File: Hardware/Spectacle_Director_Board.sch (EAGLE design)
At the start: 56 parts, among them J1 AUDIO-JACK3, J2 CORTEX_DEBUGPTH, Q1 2N7002PW, Q2 2N7002PW, U3 AP2112K-3.3V, U4 ATSAMD21G-A, U5 W25Q32FVSS

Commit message: Optimizing routing
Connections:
- new net USB_ID: JP15.ID
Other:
- moved on the sheet: JP15
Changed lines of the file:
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@@
 <instance part="GND26" gate="1" x="30.48" y="149.86"/>
 <instance part="F1" gate="G$1" x="38.1" y="175.26"/>
-<instance part="JP15" gate="G$1" x="20.32" y="167.64" rot="MR0"/>
+<instance part="JP15" gate="G$1" x="20.32" y="162.56" rot="MR0"/>
 <instance part="GND15" gate="1" x="73.66" y="160.02"/>
 <instance part="C7" gate="G$1" x="68.58" y="167.64" rot="MR0"/>
@@
 <segment>
 <pinref part="GND26" gate="1" pin="GND"/>
-<wire x1="30.48" y1="162.56" x2="30.48" y2="152.4" width="0.1524" layer="91"/>
-<wire x1="30.48" y1="162.56" x2="27.94" y2="162.56" width="0.1524" layer="91"/>
+<wire x1="30.48" y1="157.48" x2="30.48" y2="152.4" width="0.1524" layer="91"/>
+<wire x1="30.48" y1="157.48" x2="27.94" y2="157.48" width="0.1524" layer="91"/>
 <pinref part="JP15" gate="G$1" pin="GND"/>
 </segment>
@@
 <net name="VUSB" class="0">
 <segment>
-<wire x1="27.94" y1="172.72" x2="30.48" y2="172.72" width="0.1524" layer="91"/>
-<wire x1="30.48" y1="172.72" x2="30.48" y2="175.26" width="0.1524" layer="91"/>
+<wire x1="27.94" y1="167.64" x2="30.48" y2="167.64" width="0.1524" layer="91"/>
+<wire x1="30.48" y1="167.64" x2="30.48" y2="175.26" width="0.1524" layer="91"/>
 <wire x1="30.48" y1="175.26" x2="33.02" y2="175.26" width="0.1524" layer="91"/>
 <pinref part="F1" gate="G$1" pin="1"/>
@@
 <segment>
 <pinref part="JP15" gate="G$1" pin="SHIELD"/>
-<wire x1="12.7" y1="167.64" x2="10.16" y2="167.64" width="0.1524" layer="91"/>
-<label x="10.16" y="167.64" size="1.27" layer="95" rot="R180" xref="yes"/>
+<wire x1="12.7" y1="162.56" x2="10.16" y2="162.56" width="0.1524" layer="91"/>
+<label x="10.16" y="162.56" size="1.27" layer="95" rot="R180" xref="yes"/>
 </segment>
 </net>
@@
 <segment>
 <pinref part="JP15" gate="G$1" pin="D+"/>
-<wire x1="27.94" y1="167.64" x2="30.48" y2="167.64" width="0.1524" layer="91"/>
-<label x="30.48" y="167.64" size="1.27" layer="95" xref="yes"/>
+<wire x1="27.94" y1="162.56" x2="30.48" y2="162.56" width="0.1524" layer="91"/>
+<label x="30.48" y="162.56" size="1.27" layer="95" xref="yes"/>
 </segment>
 </net>
@@
 <segment>
 <pinref part="JP15" gate="G$1" pin="D-"/>
-<wire x1="27.94" y1="170.18" x2="30.48" y2="170.18" width="0.1524" layer="91"/>
-<label x="30.48" y="170.18" size="1.27" layer="95" xref="yes"/>
+<wire x1="27.94" y1="165.1" x2="30.48" y2="165.1" width="0.1524" layer="91"/>
+<label x="30.48" y="165.1" size="1.27" layer="95" xref="yes"/>
 </segment>
 </net>
@@
 </segment>
 </net>
+<net name="USB_ID" class="0">
+<segment>
+<pinref part="JP15" gate="G$1" pin="ID"/>
+<wire x1="27.94" y1="160.02" x2="30.48" y2="160.02" width="0.1524" layer="91"/>
+</segment>
+</net>

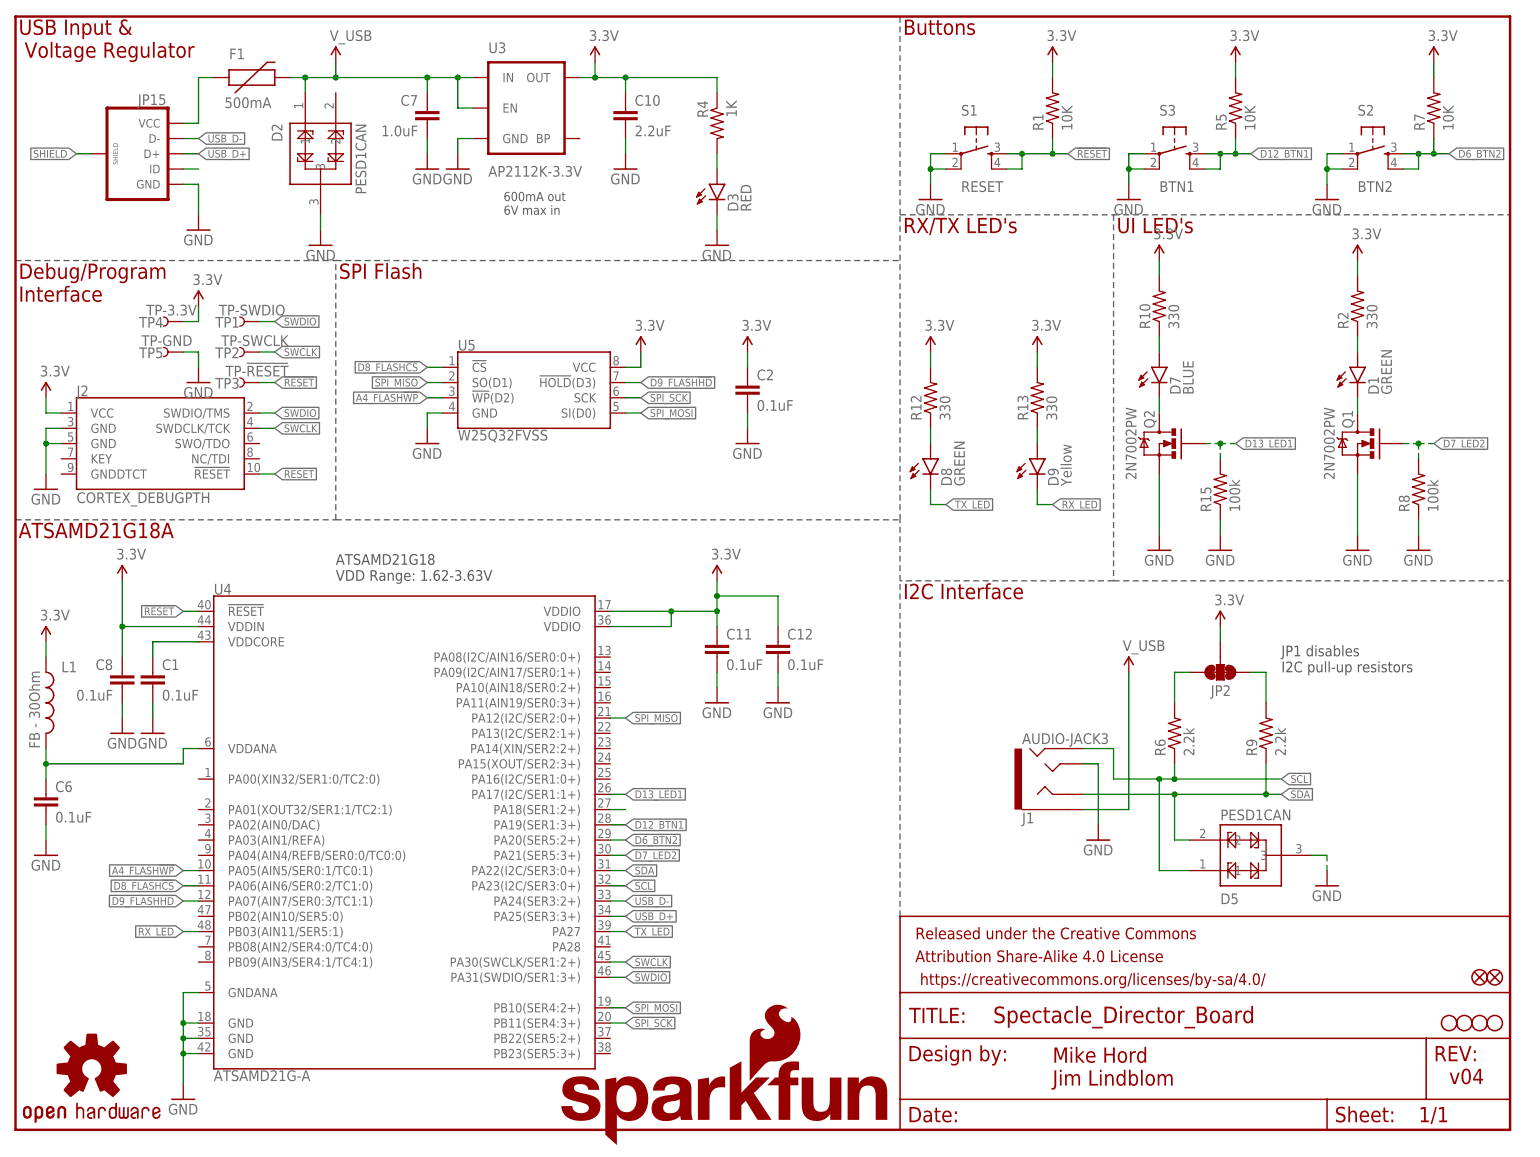
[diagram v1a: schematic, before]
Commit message: Adding second trrs for program, usb out control
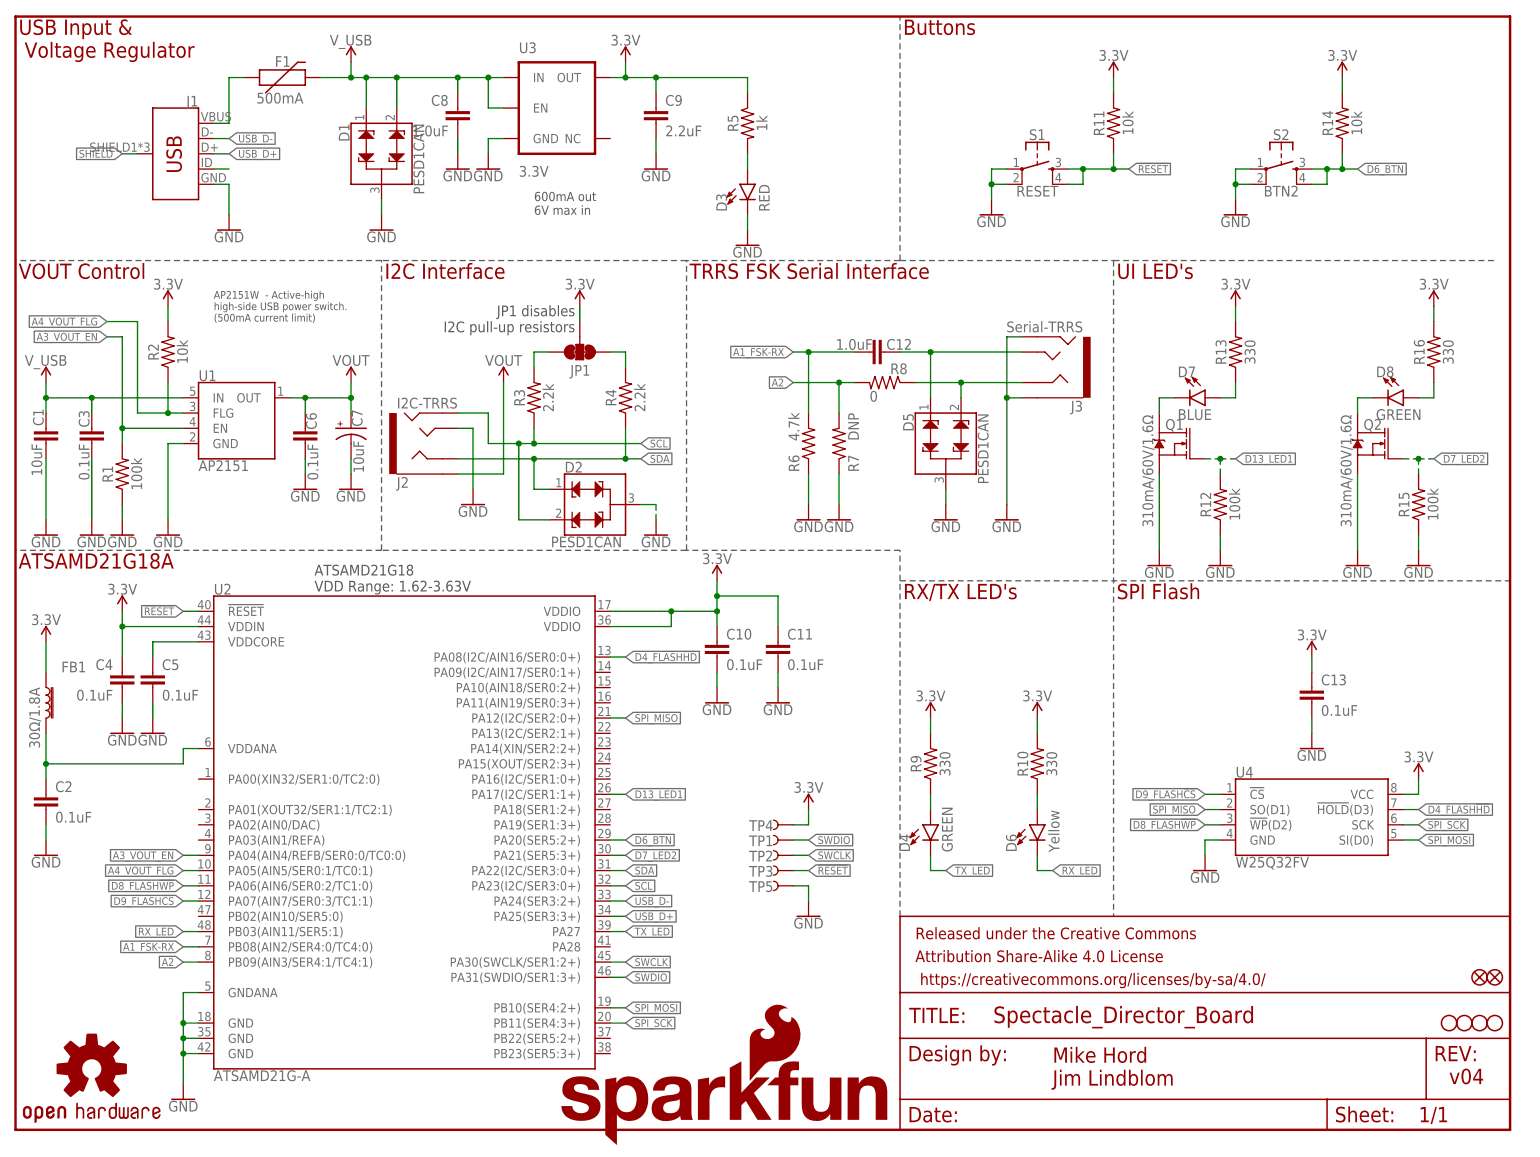
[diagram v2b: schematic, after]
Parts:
- removed D9: Yellow, SparkFun-LED:LED-YELLOW0603
- removed JP15: (no value), SparkFun-Connectors:USB_MICROB_PLUGCONN-11752
- removed JP2: JUMPER-SMT_3_2-NC_TRACE_SILK, SparkFun-Jumpers:JUMPER-SMT_3_2-NC_TRACE_SILK
- removed L1: FB - 30Ohm, SparkFun-Passives:INDUCTOR0603
- removed S3: BTN1, SparkFun-Electromechanical:SWITCH_SPST_4_PINRECT
- removed U5: W25Q32FVSS, SparkFun-DigitalIC:W25Q32FVSS
- added C13, C3, C4, C5: 0.1uF, SparkFun-Capacitors:0.1UF-0603-25V-(+80/-20%)
- added C9: 2.2uF, SparkFun-Capacitors:2.2UF-0603-10V-20%
- added D4: GREEN, SparkFun-LED:LED-GREEN0603
- added D6: Yellow, SparkFun-LED:LED-YELLOW0603
- added FB1: 30Ω/1.8A, SparkFun-Inductors:FERRITE_BEAD-0603
- added J3: Serial-TRRS, SparkFun-Connectors:AUDIO_JACK_TRRSSMD_RA
- added JP1: JUMPER-SMT_3_2-NC_TRACE_SILK, SparkFun-Jumpers:JUMPER-SMT_3_2-NC_TRACE_SILK
- added R11, R14: 10k, SparkFun-Resistors:10KOHM-0603-1/10W-1%
- added R16: 330, SparkFun-Resistors:330OHM-0603-1/10W-1%
- added R3: 2.2k, SparkFun-Resistors:2.2KOHM-0603-1/10W-1%
- added U1: AP2151, spectacle-director-temp:AP2151W
- added U2: ATSAMD21G-A, SparkFun-IC-Microcontroller:ATSAMD21G-A
- C1: value 0.1uF -> 10uF; device SparkFun-Capacitors:0.1UF-25V(+80/-20%)(0603) -> SparkFun-Capacitors:10UF-0805-10V-10%
- C10: value 2.2uF -> 0.1uF; device SparkFun-Capacitors:2.2UF-10V-20%(0603) -> SparkFun-Capacitors:0.1UF-0603-25V-(+80/-20%)
- C11, C2, C6: device SparkFun-Capacitors:0.1UF-25V(+80/-20%)(0603) -> SparkFun-Capacitors:0.1UF-0603-25V-(+80/-20%)
- C12: value 0.1uF -> 1.0uF; device SparkFun-Capacitors:0.1UF-25V(+80/-20%)(0603) -> SparkFun-Capacitors:1.0UF-0603-16V-10%
- C7: value 1.0uF -> 10uF; device SparkFun-Capacitors:1.0UF-25V-+80/-20(0805)" -> SparkFun-Capacitors:10UF-POLAR-EIA3216-16V-10%(TANT)
- C8: value 0.1uF -> 1.0uF; device SparkFun-Capacitors:0.1UF-25V(+80/-20%)(0603) -> SparkFun-Capacitors:1.0UF-0805-25V-(+80/-20%)
- D1: value GREEN -> PESD1CAN; device SparkFun-LED:LED-GREEN0603 -> SparkFun-DiscreteSemi:PESD1CAN
- H1, H2, H3, H4: device SparkFun-Electromechanical:STAND-OFF -> SparkFun-Hardware:STAND-OFF
- J1: value AUDIO-JACK3 -> (none); device SparkFun-Connectors:AUDIO-JACK3 -> SparkFun-Connectors:USB_MICRO-B_FEMALE-SMT
- J2: value CORTEX_DEBUGPTH -> I2C-TRRS; device SparkFun-Connectors:CORTEX_DEBUGPTH -> SparkFun-Connectors:AUDIO_JACK_TRRSSMD_RA
- LOGO1: value SFE_LOGO_NAME.2_INCH -> OSHW-LOGOMINI; device SparkFun-Aesthetics:SFE_LOGO_NAME.2_INCH -> SparkFun-Aesthetics:OSHW-LOGOMINI
- LOGO2: value OSHW-LOGOMINI -> SFE_LOGO_NAME.2_INCH; device SparkFun-Aesthetics:OSHW-LOGOMINI -> SparkFun-Aesthetics:SFE_LOGO_NAME.2_INCH
- LOGO3: value SFE_LOGO_FLAME.2EXP -> SFE_LOGO_FLAME.1COP; device SparkFun-Aesthetics:SFE_LOGO_FLAME.2EXP -> SparkFun-Aesthetics:SFE_LOGO_FLAME.1COP
- Q1, Q2: value 2N7002PW -> 310mA/60V/1.6Ω; device SparkFun-DiscreteSemi:MOSFET-NCHANNEL2N7002PW -> SparkFun-DiscreteSemi:MOSFET-NCH-2N7002PW
- R1: value 10K -> 100k; device SparkFun-Resistors:10KOHM-1/10W-1%(0603)0603 -> SparkFun-Resistors:100KOHM-0603-1/10W-1%
- R10, R13: device SparkFun-Resistors:330OHM1/10W1%(0603) -> SparkFun-Resistors:330OHM-0603-1/10W-1%
- R12: value 330 -> 100k; device SparkFun-Resistors:330OHM1/10W1%(0603) -> SparkFun-Resistors:100KOHM-0603-1/10W-1%
- R15: device SparkFun-Resistors:100KOHM-1/10W-1%(0603) -> SparkFun-Resistors:100KOHM-0603-1/10W-1%
- R2: value 330 -> 10k; device SparkFun-Resistors:330OHM1/10W1%(0603) -> SparkFun-Resistors:10KOHM-0603-1/10W-1%
- R4: value 1K -> 2.2k; device SparkFun-Resistors:1KOHM-1/10W-1%(0603) -> SparkFun-Resistors:2.2KOHM-0603-1/10W-1%
- R5: value 10K -> 1k; device SparkFun-Resistors:10KOHM-1/10W-1%(0603)0603 -> SparkFun-Resistors:1KOHM-0603-1/10W-1%
- R6: value 2.2k -> 4.7k; device SparkFun-Resistors:2.2KOHM-1/10W-1%(0603) -> SparkFun-Resistors:4.7KOHM-0603-1/10W-1%
- R7: value 10K -> DNP; device SparkFun-Resistors:10KOHM-1/10W-1%(0603)0603 -> SparkFun-Resistors:4.7KOHM-0603-1/10W-1%
- R8: value 100k -> 0; device SparkFun-Resistors:100KOHM-1/10W-1%(0603) -> SparkFun-Resistors:0OHM-0603-1/10W-5%
- R9: value 2.2k -> 330; device SparkFun-Resistors:2.2KOHM-1/10W-1%(0603) -> SparkFun-Resistors:330OHM-0603-1/10W-1%
- S1, S2: device SparkFun-Electromechanical:SWITCH_SPST_4_PINRECT -> SparkFun-Switches:MOMENTARY-SWITCH-SPST-2-SMD-4.6X2.8MM
- U3: value AP2112K-3.3V -> 3.3V; device SparkFun-PowerIC:V_REG_LDOSMD -> SparkFun-IC-Power:V_REG_AP2112K-3.3V
- U4: value ATSAMD21G-A -> W25Q32FV; device samd21-temp:ATSAMD21G-A -> SparkFun-IC-Memory:W25Q32FVSS
- renumbered FRAME2 to FRAME1
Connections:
- removed net A4_FLASH!WP!: U4.PA05(AIN5/SER0:1/TC0:1), U5.!WP!(D2)
- removed net D10: U4.PA18(SER1:2+)
- removed net D12_BTN1: R5.1, S3.3, S3.4, U4.PA19(SER1:3+)
- removed net D6_BTN2: R7.1, S2.3, S2.4, U4.PA20(SER5:2+)
- removed net D8_FLASH!CS!: U4.PA06(AIN6/SER0:2/TC1:0), U5.!CS!
- removed net D9_FLASH!HD!: U4.PA07(AIN7/SER0:3/TC1:1), U5.!HOLD!(D3)
- new net A1_FSK-RX: C12.2, R6.2, U2.PB08(AIN2/SER4:0/TC4:0)
- new net A2: R7.2, R8.2, U2.PB09(AIN3/SER4:1/TC4:1)
- new net A3_VOUT_EN: R1.2, U1.EN, U2.PA04(AIN4/REFB/SER0:0/TC0:0)
- new net A4_VOUT_FLG: R2.1, U1.FLG, U2.PA05(AIN5/SER0:1/TC0:1)
- new net D4_FLASH!HD!: U2.PA08(I2C/AIN16/SER0:0+), U4.!HOLD!(D3)
- new net D6_BTN: R14.1, S2.3, S2.4, U2.PA20(SER5:2+)
- new net D8_FLASH!WP!: U2.PA06(AIN6/SER0:2/TC1:0), U4.!WP!(D2)
- new net D9_FLASH!CS!: U2.PA07(AIN7/SER0:3/TC1:1), U4.!CS!
- new net RING1-RIGHT: D5.2, J3.RING1, R8.1
- new net TIP-LEFT: C12.1, D5.1, J3.TIP
- new net VOUT: C6.1, C7.+, J2.EARTH, U1.OUT
- net !RESET: now also R11.1, U2.!RESET!; no longer J2.!RESET, R1.1, U4.!RESET!
- net 3.3V: now also C13.1, C4.1, C9.1, FB1.1, JP1.2, R11.2, R14.2, R16.2, R5.1, R9.2, U2.VDDIN, U2.VDDIO@17, U2.VDDIO@36, U4.VCC; no longer C12.1, C2.1, C8.1, J2.VCC, JP2.2, L1.1, R1.2, R12.2, R4.1, R5.2, R7.2, U4.VDDIN, U4.VDDIO@17, U4.VDDIO@36, U5.VCC
- net D13_LED1: now also Q1.G, R12.2, U2.PA17(I2C/SER1:1+); no longer Q2.G, R15.2, U4.PA17(I2C/SER1:1+)
- net D7_LED2: now also Q2.G, R15.2, U2.PA21(SER5:3+); no longer Q1.G, R8.2, U4.PA21(SER5:3+)
- net GND: now also C13.2, C3.2, C4.2, C5.2, C7.-, C9.2, D1.3, J1.GND, J2.TIP, J3.EARTH, J3.RING2, R1.1, R12.1, R6.1, R7.1, U1.GND, U2.GND@18, U2.GND@35, U2.GND@42, U2.GNDANA, U4.GND; no longer C12.2, C7.2, J1.TIP, J2.GND@3, J2.GND@5, JP15.GND, R8.1, S3.1, S3.2, U4.GND@18, U4.GND@35, U4.GND@42, U4.GNDANA, U5.GND
- net N$1: now also D8.A, R16.1; no longer D1.A, R2.1
- net N$10: now also Q1.D; no longer Q2.D
- net N$11: now also D4.A, R9.1; no longer D8.A, R12.1
- net N$12: now also D6.A, R10.1; no longer D9.A, R13.1
- net N$2: now also R5.2; no longer R4.2
- net N$4: now also JP1.3, R3.2; no longer JP2.3, R6.2
- net N$5: now also JP1.1, R4.2; no longer JP2.1, R9.2
- net N$7: now also D8.C, Q2.D; no longer D1.C, Q1.D
- net N$9: now also R13.1; no longer R10.1
- net RX_LED: now also D6.C, U2.PB03(AIN11/SER5:1); no longer D9.C, U4.PB03(AIN11/SER5:1)
- net SCL: now also D2.2, J2.RING2, R3.1, U2.PA23(I2C/SER3:0+); no longer D5.1, J1.RING2, R6.1, U4.PA23(I2C/SER3:0+)
- net SDA: now also D2.1, J2.RING1, R4.1, U2.PA22(I2C/SER3:0+); no longer D5.2, J1.RING1, R9.1, U4.PA22(I2C/SER3:0+)
- net SHIELD: now also J1.SHIELD; no longer JP15.SHIELD
- net SPI_MISO: now also U2.PA12(I2C/SER2:0+), U4.SO(D1); no longer U4.PA12(I2C/SER2:0+), U5.SO(D1)
- net SPI_MOSI: now also U2.PB10(SER4:2+), U4.SI(D0); no longer U4.PB10(SER4:2+), U5.SI(D0)
- net SPI_SCK: now also U2.PB11(SER4:3+), U4.SCK; no longer U4.PB11(SER4:3+), U5.SCK
- net SWCLK: now also U2.PA30(SWCLK/SER1:2+); no longer J2.SWDCLK/TCK, U4.PA30(SWCLK/SER1:2+)
- net SWDIO: now also U2.PA31(SWDIO/SER1:3+); no longer J2.SWDIO/TMS, U4.PA31(SWDIO/SER1:3+)
- net TX_LED: now also D4.C, U2.PA27; no longer D8.C, U4.PA27
- net USB_D+: now also J1.D+, U2.PA25(SER3:3+); no longer JP15.D+, U4.PA25(SER3:3+)
- net USB_D-: now also J1.D-, U2.PA24(SER3:2+); no longer JP15.D-, U4.PA24(SER3:2+)
- net USB_ID: now also J1.ID; no longer JP15.ID
- net VDDANA: now also C2.1, FB1.2, U2.VDDANA; no longer C6.1, L1.2, U4.VDDANA
- net VDDCORE: now also C5.1, U2.VDDCORE; no longer C1.1, U4.VDDCORE
- net VUSB: now also J1.VBUS; no longer JP15.VCC
- net V_USB: now also C1.1, C3.1, C8.1, D1.1, D1.2, U1.IN; no longer C7.1, D2.1, J1.EARTH
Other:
- note added: "AP2151W - Active-high high-side USB power switch. (500mA current limit)"
- note added: "TRRS FSK Serial Interface"
- note added: "VOUT Control"
- note removed: "Debug/Program Interface"
- moved on the sheet: C1, C10, C11, C12, C2, C6, C8, F1, R1, R10, R12, R13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
